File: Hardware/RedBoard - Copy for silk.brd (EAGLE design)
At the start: 68.6 x 53.3 mm, 73 parts, among them IC3 LM1117, J1 AMP FCI 10103594-0001LF, J2 ISP, J3 POWER_JACKSUPER_BOMB_DIGITY, Q1 1A/60V/500mΩ, Q2 2N7002PW, Q3 2N7002PW, U1 CH340C, U3 AP2112-3.3V, U4 ATMEGA328P_TQFP, Y1 16MHz

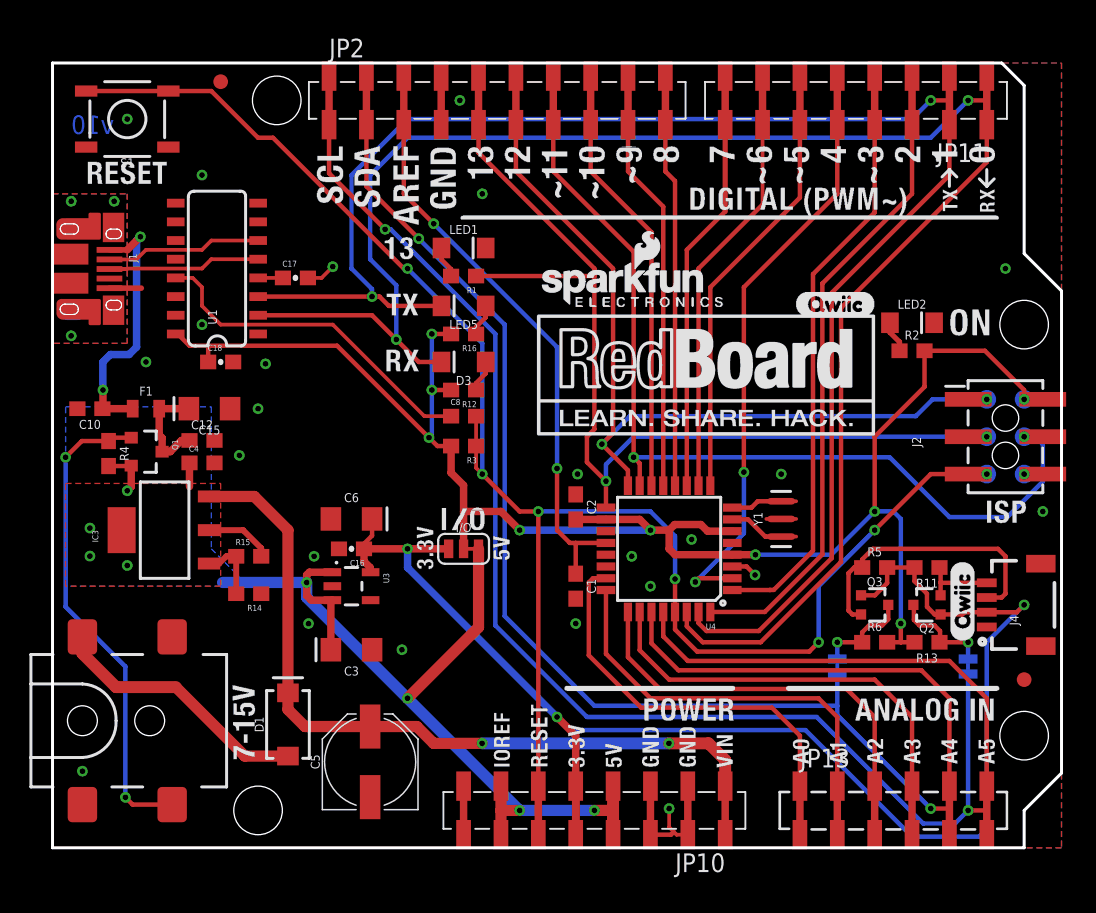
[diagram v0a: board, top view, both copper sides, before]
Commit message: Design Review fixes to silk and componenet placement
Design Review fixes to silk and componenet placement
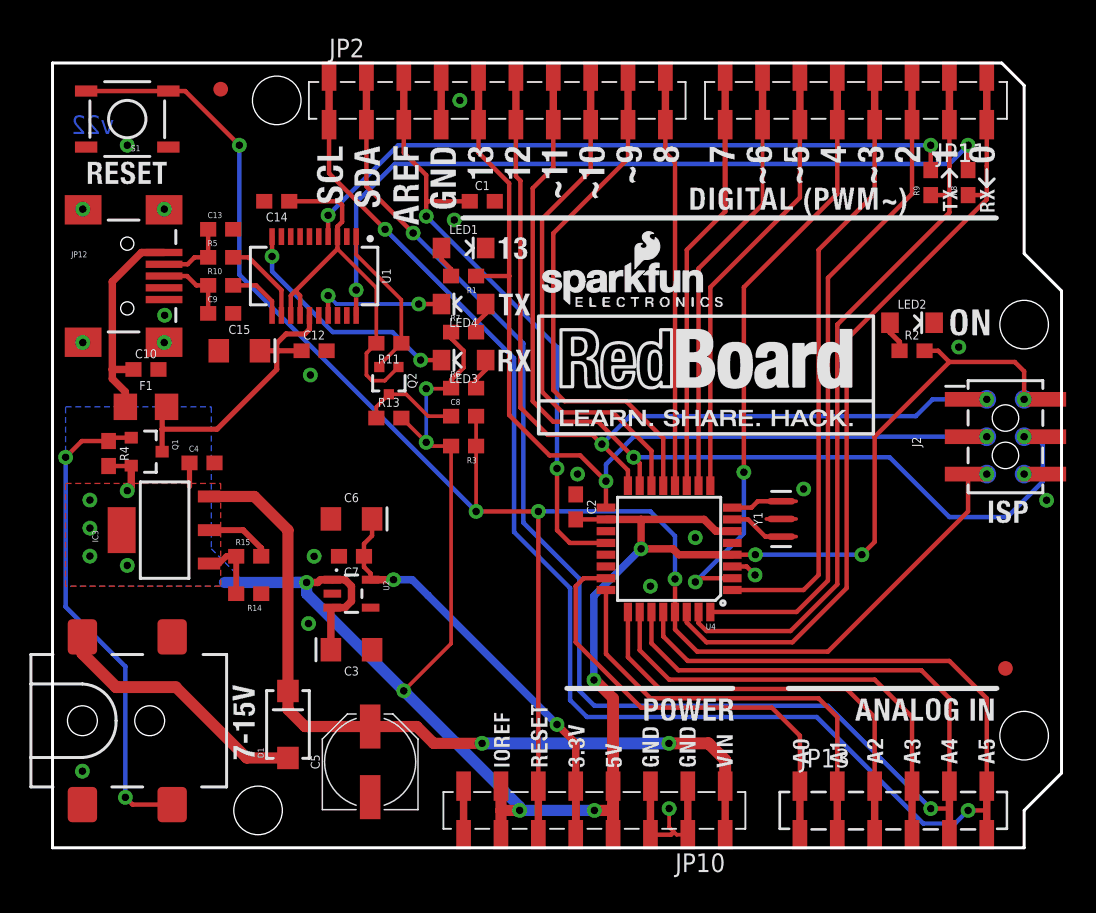
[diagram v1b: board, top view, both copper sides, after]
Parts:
- removed C16: 1.0uF, SparkFun-Capacitors:0603-CAP
- removed C17: 10nF, SparkFun-Capacitors:0603-CAP
- removed C18: 0.1uF, SparkFun-Capacitors:0603-CAP
- removed D3: Yellow, SparkFun-LED:LED-1206-HIDDENSILK
- removed I/O: (no value), SparkFun-Jumpers:SMT-JUMPER_3_1-NC_TRACE_SILK
- removed J1: AMP FCI 10103594-0001LF, SparkFun-Connectors:USB-MICROB-PTH-MILL
- removed J4: (no value), SparkFun-Connectors:1X04_1MM_RA
- removed JP14: (no value), SparkFun-Jumpers:SMT-JUMPER_2_NC_TRACE_SILK
- removed LED5: GREEN, SparkFun-LED:LED-1206-HIDDENSILK
- removed LOGO1: REVISION, SparkFun-Aesthetics:REVISION
- removed Q3: 2N7002PW, SparkFun-DiscreteSemi:SOT323
- removed R12, R16: 4.7k, SparkFun-Resistors:0603
- removed U$1, U$2, U$3: (no value), Labels-0_04:(QWIIC)
- removed U$4: (no value), buzzard_labels_J12:J120
- removed U$9: (no value), buzzard_labels_J14:J140
- removed U3: AP2112-3.3V, SparkFun-PowerIC:SOT23-5
- added C13, C9: 47pF, SparkFun-Capacitors:0603
- added C14: 0.1uF, SparkFun-Capacitors:0603
- added C7: 1.0uF, SparkFun-Capacitors:0603
- added LED3: Red, SparkFun-LED:LED-1206
- added LED4: Yellow, SparkFun-LED:LED-1206
- added R10: 27, SparkFun-Resistors:0603
- added R7, R8, R9: 1k, SparkFun-Resistors:0603
- added U2: MIC5205, SparkFun-PowerIC:SOT23-5
- D1: value 1A/40V/500mV -> MBRA140
- F1: value PPTC_6V500MA -> 6V/0.5A; device SparkFun-Fuses:0805 -> SparkFun-Fuses:1206
- J2: value ISP -> ICSP
- JP10: value (none) -> JP10
- JP11: value JP11 -> IOL
- JP12: value (none) -> USB-MINIB-5PIN; device SparkFun-Jumpers:SMT-JUMPER_2_NC_TRACE_SILK -> SparkFun-Connectors:USB-MINIB
- JP13: value (none) -> AD
- LED1: device SparkFun-LED:LED-1206-HIDDENSILK -> SparkFun-LED:LED-1206
- LED2: value GREEN -> Green; device SparkFun-LED:LED-1206-HIDDENSILK -> SparkFun-LED:LED-1206
- R1: value 4.7k -> 1k
- R11, R13: value 2.2k -> 10k
- R2: value 10k -> 4.7k
- R5: value 2.2k -> 27
- R6: value 2.2k -> 1k
- S1: device SparkFun-Switches:TACTILE_SWITCH_SMD_5.2MM -> SparkFun-Electromechanical:TACTILE-SWITCH-SMD
- U1: value CH340C -> FT231XS; device SparkFun-IC-Comms:SO016 -> SparkFun-IC-Comms:SSOP20_L
- moved JP12 63.0 mm to (5.08, 38.9), flipped to the top, turned to 0 degrees
- moved R5 49.2 mm to (11.4, 40.1)
- moved Q2 39.6 mm to (22.9, 31.8), turned to 180 degrees
- moved R11 39.6 mm to (22.9, 34.3)
- moved R13 39.6 mm to (22.9, 29.2), turned to 0 degrees
- moved R6 32.8 mm to (27.9, 31.2)
- moved C1 26.9 mm to (29.2, 43.9), turned to 0 degrees
- moved FRAME2 12.0 mm to (1.27, -39.4)
- moved C12 9.76 mm to (17.8, 33.8)
- moved U1 6.62 mm to (17.8, 38.9), turned to 180 degrees
- moved C10 4.65 mm to (6.35, 32.5), turned to 0 degrees
- moved C15 4.43 mm to (12.7, 33.8), turned to 0 degrees
- moved JP8 1.48 mm to (64.8, 12.2)
- moved JP9 0.51 mm to (11.4, 51.6)
- moved F1 0.13 mm to (6.35, 30.0)
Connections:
- removed net !DTR: C8.1, U1.13
- removed net LV_SCL: J4.4, Q2.2, R11.1
- removed net LV_SDA: J4.3, Q3.2, R5.1
- removed net N$13: J1.D-, U1.6
- removed net N$14: J1.D+, U1.5
- removed net N$5: LED5.A, R16.1
- removed net N$9: D3.A, R12.1
- removed net SHLD: J1.SHIELD, J1.SHIELD10, J1.SHIELD2, J1.SHIELD3, J1.SHIELD4, J1.SHIELD5, J1.SHIELD6, J1.SHIELD7, J1.SHIELD8, J1.SHIELD9
- removed net VCC: C18.1, C2.2, I/O.2, J2.2, R12.2, R13.2, R16.2, R2.2, R3.2, R6.2, TP1.P$1, U1.16, U4.18, U4.4, U4.6
- new net 3.3V_F: C14.1, Q2.1, R11.2, U1.13, U1.14, U1.3
- new net D+: C9.1, JP12.D+, R10.1
- new net D-: C13.1, JP12.D-, R5.1
- new net DTR: C8.1, Q2.3, R13.1
- new net FTDI_DTR: Q2.2, R11.1, U1.1
- new net N$10: LED4.A, R7.2
- new net RXD: R9.2, U1.4
- new net RXLED: LED4.C, U1.17
- new net TXD: R8.2, U1.20
- new net TXLED: LED3.C, U1.10
- net 3.3V: now also C7.1, U2.5; no longer C16.1, I/O.1, J4.2, Q2.1, Q3.1, R11.2, R5.2, U3.5
- net 5V: now also C2.2, J2.2, R13.2, R2.2, R3.2, R6.1, R7.1, TP1.P$1, U2.1, U2.3, U4.18, U4.4, U4.6; no longer I/O.3, U3.1, U3.3
- net AD4/SDA: no longer JP14.2
- net AD5/SCL: no longer JP12.2
- net GND: now also C13.2, C14.2, C7.2, C9.2, JP12.GND, JP12.MTN1, JP12.MTN2, JP12.MTN3, JP12.MTN4, U1.16, U1.6, U2.2; no longer C16.2, C17.2, C18.2, J1.GND, J4.1, U1.1, U3.2
- net N$6: now also R5.2, U1.12; no longer C17.1, U1.4
- net N$7: now also R10.2, U1.11; no longer JP12.1, Q2.3, R13.1
- net N$8: now also LED3.A, R6.2; no longer JP14.1, Q3.3, R6.1
- net RX-I: now also R8.1; no longer D3.C, U1.2
- net TX-O: now also R9.1; no longer LED5.C, U1.3
- net USBVCC: now also U1.15
- net VUSB: now also JP12.VBUS; no longer J1.VBUS
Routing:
- net VCC: track 115.5 -> 0.00 mm, vias 9 -> 0
- net 5V: track 73.9 -> 167.1 mm, vias 8 -> 16
- net 3.3V: track 101.5 -> 29.3 mm, vias 3 -> 2
- net RX-I: track 122.3 -> 50.4 mm, vias 2 -> 0
- net TX-O: track 114.1 -> 50.7 mm, vias 2 -> 0
- net TXD: track 0.00 -> 52.6 mm, vias 0 -> 2
- net RXD: track 0.00 -> 46.1 mm, vias 0 -> 2
- net 3.3V_F: track 0.00 -> 27.1 mm
- net !DTR: track 23.4 -> 0.00 mm
- net LV_SDA: track 19.3 -> 0.00 mm
- net TXLED: track 0.00 -> 16.4 mm, vias 0 -> 2
- net AD5/SCL: track 125.5 -> 111.1 mm
- net USBVCC: track 7.20 -> 20.8 mm
- net FTDI_DTR: track 0.00 -> 10.8 mm
- net N$13: track 10.6 -> 0.00 mm
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- removed copper zone on layer 1, net SHLD
- removed copper zone on layer 16, net SHLD
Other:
- board text added: "Based on Arduino by: M.Banzi, D.Cuartielles, T.Igoe, G.Martino, D.Mellis"
- board text added: "ITALY"
- board text added: "J.Lindblom"
- board text added: "MADE IN"
- board text added: "v22"
- board text removed: "Based on Arduino by: M. Banzi, D. Cuartielles, T. Igoe, G. Martino, D. Mellis"
- board text removed: "J. Lindblom, N. Seidle"
- board text removed: "v10"
